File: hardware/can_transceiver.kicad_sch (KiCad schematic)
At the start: 4 parts, among them J3 CAN, U5 MCP2558FD-xSN

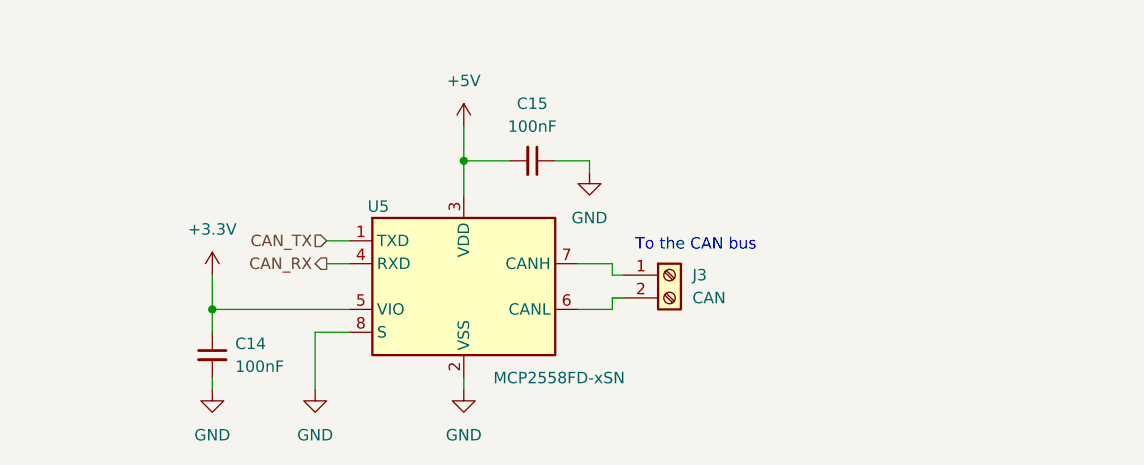
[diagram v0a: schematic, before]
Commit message: Improve the CAN transceiver circuit
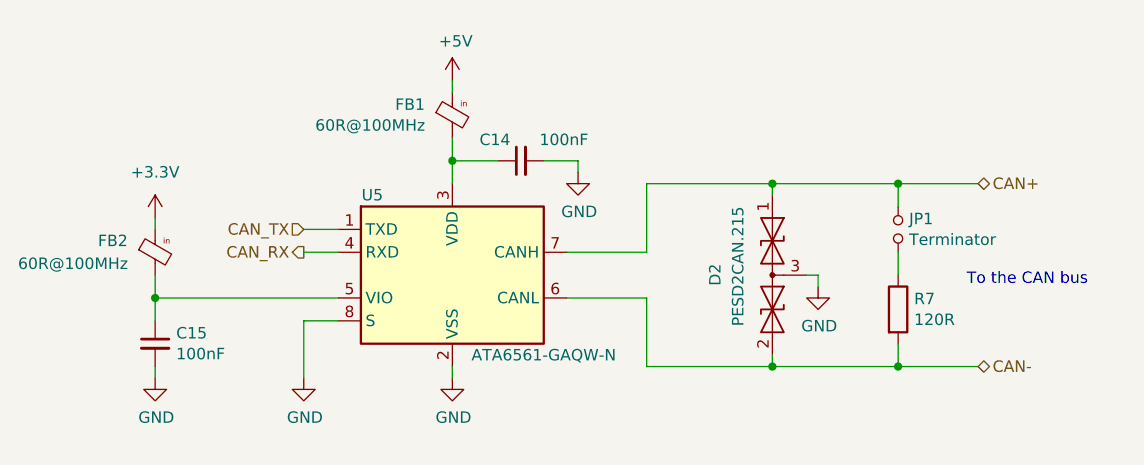
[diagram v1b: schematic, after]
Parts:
- removed J3: CAN, symbol Connector:Screw_Terminal_01x02
- added D2: PESD2CAN.215, Package_TO_SOT_SMD:SOT-23, symbol Local_Library:D_TVS_x2_AAC-Device
- added FB1, FB2: 60R@100MHz, Inductor_SMD:L_0603_1608Metric, symbol Local_Library:Ferrite_Bead_Small_PWR-PUTM_KICAD_SYMBOLS
- added JP1: Terminator, Connector_PinHeader_2.54mm:PinHeader_1x02_P2.54mm_Vertical, symbol Local_Library:Jumper_NO_Small-Device
- added R7: 120R, Resistor_SMD:R_0603_1608Metric, symbol Device:R
- C14, C15: footprint (none) -> Capacitor_SMD:C_0603_1608Metric
- U5: value MCP2558FD-xSN -> ATA6561-GAQW-N
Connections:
- net +3.3V: now also FB2.1; no longer C14.1, U5.5 (VIO)
- net +5V: now also FB1.1; no longer C15.2, U5.3 (VDD)
- net GND: now also C15.2, D2.3 (common); no longer C15.1
- net CAN-: now reaches U5.6 (CANL)
- net CAN-: now also D2.2 (A2), R7.2
- net CAN+: now reaches U5.7 (CANH)
- net CAN+: now also D2.1 (A1), JP1.1
- new net: C15.1, FB2.2, U5.5 (VIO)
- new net: JP1.2, R7.1
- new net: C14.1, FB1.2, U5.3 (VDD)
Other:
- company: PUT MotorSport -> PUT Motorsport

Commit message: Refactor the main sheet
- Replace screw connectors with a goldpin header
- Add reset button
- Add SWD debugger header
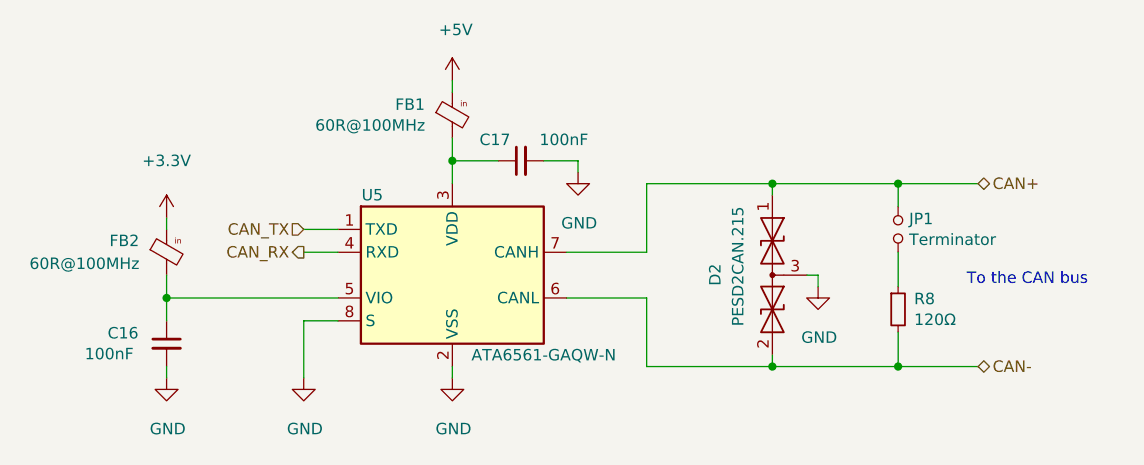
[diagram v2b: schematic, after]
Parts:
- R8: renamed from R7; value 120R -> 120Ω; symbol Device:R -> Device:R_Small
- renumbered C15 to C16, C14 to C17
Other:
- moved on the sheet: C16, FB2
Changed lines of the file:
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@@
   (junction (at 180.34 87.63) (diameter 0) (color 0 0 0 0)
   )
-  (junction (at 111.76 100.33) (diameter 0) (color 0 0 0 0)
+  (junction (at 113.03 100.33) (diameter 0) (color 0 0 0 0)
   )
   (wire (pts (xy 166.37 87.63) (xy 180.34 87.63))
@@
     (stroke (width 0) (type default) (color 0 0 0 0))
   )
-  (wire (pts (xy 194.31 105.41) (xy 194.31 107.95))
+  (wire (pts (xy 194.31 104.14) (xy 194.31 107.95))
     (stroke (width 0) (type default) (color 0 0 0 0))
   )
@@
     (stroke (width 0) (type default) (color 0 0 0 0))
   )
-  (wire (pts (xy 111.76 100.33) (xy 111.76 97.79))
+  (wire (pts (xy 194.31 95.25) (xy 194.31 99.06))
+    (stroke (width 0) (type default) (color 0 0 0 0))
+  )
+  (wire (pts (xy 113.03 100.33) (xy 113.03 97.79))
     (stroke (width 0) (type default) (color 0 0 0 0))
   )
@@
     (stroke (width 0) (type default) (color 0 0 0 0))
   )
-  (wire (pts (xy 111.76 100.33) (xy 111.76 102.87))
+  (wire (pts (xy 113.03 100.33) (xy 113.03 102.87))
     (stroke (width 0) (type default) (color 0 0 0 0))
   )
@@
     (stroke (width 0) (type default) (color 0 0 0 0))
   )
-  (wire (pts (xy 111.76 100.33) (xy 132.08 100.33))
+  (wire (pts (xy 113.03 100.33) (xy 132.08 100.33))
     (stroke (width 0) (type default) (color 0 0 0 0))
   )
@@
     (stroke (width 0) (type default) (color 0 0 0 0))
   )
-  (wire (pts (xy 111.76 91.44) (xy 111.76 92.71))
+  (wire (pts (xy 113.03 91.44) (xy 113.03 92.71))
     (stroke (width 0) (type default) (color 0 0 0 0))
   )
@@
     (stroke (width 0) (type default) (color 0 0 0 0))
   )
-  (wire (pts (xy 194.31 95.25) (xy 194.31 97.79))
-    (stroke (width 0) (type default) (color 0 0 0 0))
-  )
-  (wire (pts (xy 111.76 109.22) (xy 111.76 107.95))
+  (wire (pts (xy 113.03 109.22) (xy 113.03 107.95))
     (stroke (width 0) (type default) (color 0 0 0 0))
   )
@@
     (effects (font (size 1.27 1.27)) (justify right))
   )
-  (symbol (lib_id "Local_Library:Ferrite_Bead_Small_PWR-PUTM_KICAD_SYMBOLS") (at 111.76 95.25 0) (unit 1)
-    (in_bom yes) (on_board yes)
-    (property "Reference" "FB2" (id 0) (at 105.41 93.98 0)
-      (effects (font (size 1.27 1.27)) (justify left))
-    )
-    (property "Value" "60R@100MHz" (id 1) (at 96.52 96.52 0)
-      (effects (font (size 1.27 1.27)) (justify left))
-    )
-    (property "Footprint" "Inductor_SMD:L_0603_1608Metric" (id 2) (at 109.982 95.25 90)
-      (effects (font (size 1.27 1.27)) hide)
-    )
-    (property "Datasheet" "~" (id 3) (at 111.76 95.25 0)
+  (symbol (lib_id "Local_Library:Ferrite_Bead_Small_PWR-PUTM_KICAD_SYMBOLS") (at 113.03 95.25 0) (unit 1)
+    (in_bom yes) (on_board yes)
+    (property "Reference" "FB2" (id 0) (at 106.68 93.98 0)
+      (effects (font (size 1.27 1.27)) (justify left))
+    )
+    (property "Value" "60R@100MHz" (id 1) (at 97.79 96.52 0)
+      (effects (font (size 1.27 1.27)) (justify left))
+    )
+    (property "Footprint" "Inductor_SMD:L_0603_1608Metric" (id 2) (at 111.252 95.25 90)
+      (effects (font (size 1.27 1.27)) hide)
+    )
+    (property "Datasheet" "~" (id 3) (at 113.03 95.25 0)
       (effects (font (size 1.27 1.27)) hide)
     )
@@
       (effects (font (size 1.27 1.27)) hide)
     )
-    (property "Value" "GND" (id 1) (at 128.397 113.6142 0))
+    (property "Value" "GND" (id 1) (at 128.397 114.8842 0))
     (property "Footprint" "" (id 2) (at 128.27 109.22 0)
       (effects (font (size 1.27 1.27)) hide)
@@
       (effects (font (size 1.27 1.27)) hide)
     )
-    (property "Value" "GND" (id 1) (at 185.547 103.4542 0))
+    (property "Value" "GND" (id 1) (at 185.547 104.7242 0))
     (property "Footprint" "" (id 2) (at 185.42 99.06 0)
       (effects (font (size 1.27 1.27)) hide)
@@
       (effects (font (size 1.27 1.27)) hide)
     )
-    (property "Value" "GND" (id 1) (at 144.907 113.6142 0))
+    (property "Value" "GND" (id 1) (at 144.907 114.8842 0))
     (property "Footprint" "" (id 2) (at 144.78 109.22 0)
       (effects (font (size 1.27 1.27)) hide)
@@
     (pin "1")
   )
-  (symbol (lib_id "Device:C_Small") (at 111.76 105.41 0) (unit 1)
-    (in_bom yes) (on_board yes)
-    (property "Reference" "C15" (id 0) (at 114.0968 104.2416 0)
-      (effects (font (size 1.27 1.27)) (justify left))
-    )
-    (property "Value" "100nF" (id 1) (at 114.0968 106.553 0)
-      (effects (font (size 1.27 1.27)) (justify left))
-    )
-    (property "Footprint" "Capacitor_SMD:C_0603_1608Metric" (id 2) (at 111.76 105.41 0)
-      (effects (font (size 1.27 1.27)) hide)
-    )
-    (property "Datasheet" "~" (id 3) (at 111.76 105.41 0)
+  (symbol (lib_id "Device:C_Small") (at 113.03 105.41 0) (unit 1)
+    (in_bom yes) (on_board yes)
+    (property "Reference" "C16" (id 0) (at 106.4768 104.2416 0)
+      (effects (font (size 1.27 1.27)) (justify left))
+    )
+    (property "Value" "100nF" (id 1) (at 103.9368 106.553 0)
+      (effects (font (size 1.27 1.27)) (justify left))
+    )
+    (property "Footprint" "Capacitor_SMD:C_0603_1608Metric" (id 2) (at 113.03 105.41 0)
+      (effects (font (size 1.27 1.27)) hide)
+    )
+    (property "Datasheet" "~" (id 3) (at 113.03 105.41 0)
       (effects (font (size 1.27 1.27)) hide)
     )
@@
   (symbol (lib_id "Device:C_Small") (at 152.4 85.09 90) (unit 1)
     (in_bom yes) (on_board yes)
-    (property "Reference" "C14" (id 0) (at 151.2316 82.7532 90)
+    (property "Reference" "C17" (id 0) (at 151.2316 82.7532 90)
       (effects (font (size 1.27 1.27)) (justify left))
     )
@@
     (pin "2")
   )
-  (symbol (lib_id "power:GND") (at 111.76 109.22 0) (unit 1)
-    (in_bom yes) (on_board yes)
-    (property "Reference" "#U0103" (id 0) (at 111.76 115.57 0)
-      (effects (font (size 1.27 1.27)) hide)
-    )
-    (property "Value" "GND" (id 1) (at 111.887 113.6142 0))
-    (property "Footprint" "" (id 2) (at 111.76 109.22 0)
-      (effects (font (size 1.27 1.27)) hide)
-    )
-    (property "Datasheet" "" (id 3) (at 111.76 109.22 0)
+  (symbol (lib_id "power:GND") (at 113.03 109.22 0) (unit 1)
+    (in_bom yes) (on_board yes)
+    (property "Reference" "#U0103" (id 0) (at 113.03 115.57 0)
+      (effects (font (size 1.27 1.27)) hide)
+    )
+    (property "Value" "GND" (id 1) (at 113.157 114.8842 0))
+    (property "Footprint" "" (id 2) (at 113.03 109.22 0)
+      (effects (font (size 1.27 1.27)) hide)
+    )
+    (property "Datasheet" "" (id 3) (at 113.03 109.22 0)
       (effects (font (size 1.27 1.27)) hide)
     )
@@
       (effects (font (size 1.27 1.27)) hide)
     )
-    (property "Value" "GND" (id 1) (at 158.877 90.7542 0))
+    (property "Value" "GND" (id 1) (at 158.877 92.0242 0))
     (property "Footprint" "" (id 2) (at 158.75 86.36 0)
       (effects (font (size 1.27 1.27)) hide)
@@
     (pin "1")
   )
-  (symbol (lib_id "power:+3.3V") (at 111.76 91.44 0) (unit 1)
-    (in_bom yes) (on_board yes) (fields_autoplaced)
-    (property "Reference" "#PWR0102" (id 0) (at 111.76 95.25 0)
-      (effects (font (size 1.27 1.27)) hide)
-    )
-    (property "Value" "+3.3V" (id 1) (at 111.76 86.36 0))
-    (property "Footprint" "" (id 2) (at 111.76 91.44 0)
-      (effects (font (size 1.27 1.27)) hide)
-    )
-    (property "Datasheet" "" (id 3) (at 111.76 91.44 0)
-      (effects (font (size 1.27 1.27)) hide)
-    )
-    (pin "1")
-  )
-  (symbol (lib_id "Device:R") (at 194.31 101.6 0) (unit 1)
-    (in_bom yes) (on_board yes)
-    (property "Reference" "R7" (id 0) (at 196.088 100.4316 0)
-      (effects (font (size 1.27 1.27)) (justify left))
-    )
-    (property "Value" "120R" (id 1) (at 196.088 102.743 0)
-      (effects (font (size 1.27 1.27)) (justify left))
-    )
-    (property "Footprint" "Resistor_SMD:R_0603_1608Metric" (id 2) (at 192.532 101.6 90)
+  (symbol (lib_id "power:+3.3V") (at 113.03 91.44 0) (unit 1)
+    (in_bom yes) (on_board yes)
+    (property "Reference" "#PWR0102" (id 0) (at 113.03 95.25 0)
+      (effects (font (size 1.27 1.27)) hide)
+    )
+    (property "Value" "+3.3V" (id 1) (at 113.03 85.09 0))
+    (property "Footprint" "" (id 2) (at 113.03 91.44 0)
+      (effects (font (size 1.27 1.27)) hide)
+    )
+    (property "Datasheet" "" (id 3) (at 113.03 91.44 0)
+      (effects (font (size 1.27 1.27)) hide)
+    )
+    (pin "1")
+  )
+  (symbol (lib_id "Device:R_Small") (at 194.31 101.6 0) (unit 1)
+    (in_bom yes) (on_board yes)
+    (property "Reference" "R8" (id 0) (at 196.088 100.4316 0)
+      (effects (font (size 1.27 1.27)) (justify left))
+    )
+    (property "Value" "120Ω" (id 1) (at 196.088 102.743 0)
+      (effects (font (size 1.27 1.27)) (justify left))
+    )
+    (property "Footprint" "Resistor_SMD:R_0603_1608Metric" (id 2) (at 194.31 101.6 0)
       (effects (font (size 1.27 1.27)) hide)
     )
@@
       (effects (font (size 1.27 1.27)) hide)
     )
-    (property "Value" "+5V" (id 1) (at 145.161 71.8058 0))
+    (property "Value" "+5V" (id 1) (at 145.161 70.5358 0))
     (property "Footprint" "" (id 2) (at 144.78 76.2 0)
       (effects (font (size 1.27 1.27)) hide)

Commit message: Add ADC circuit
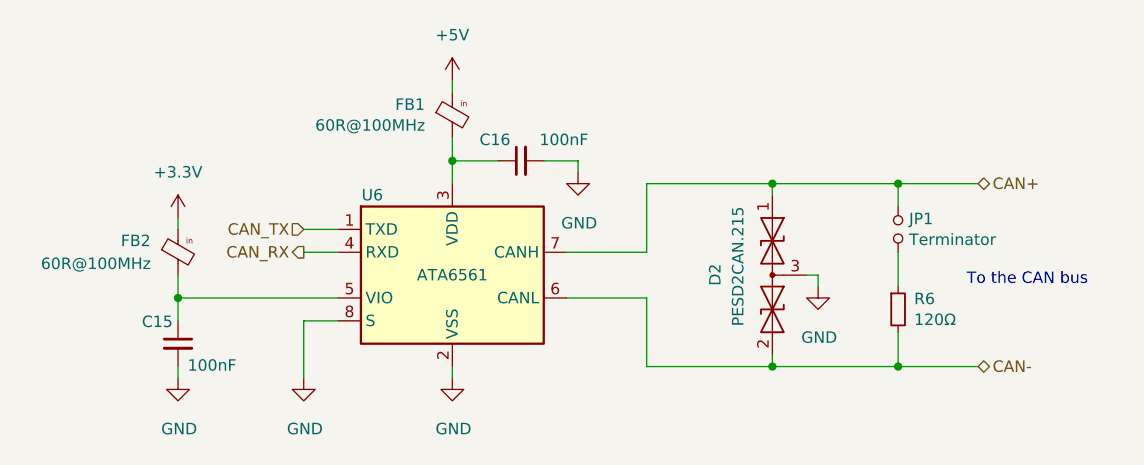
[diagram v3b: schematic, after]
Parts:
- U6: renamed from U5; value ATA6561-GAQW-N -> ATA6561
- renumbered C16 to C15, C17 to C16, R8 to R6
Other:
- moved on the sheet: C15, FB2
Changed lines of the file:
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@@
   (title_block
     (title "CAN Transceiver")
-    (date "2022-11-21")
+    (date "2022-12-04")
     (rev "0.1.0")
     (company "PUT Motorsport")
+    (comment 1 "Author: I. Kajdan")
   )
   (junction (at 180.34 107.95) (diameter 0) (color 0 0 0 0)
@@
   (junction (at 180.34 87.63) (diameter 0) (color 0 0 0 0)
   )
-  (junction (at 113.03 100.33) (diameter 0) (color 0 0 0 0)
+  (junction (at 114.3 100.33) (diameter 0) (color 0 0 0 0)
   )
   (wire (pts (xy 166.37 87.63) (xy 180.34 87.63))
@@
     (stroke (width 0) (type default) (color 0 0 0 0))
   )
-  (wire (pts (xy 113.03 100.33) (xy 113.03 97.79))
+  (wire (pts (xy 114.3 100.33) (xy 114.3 97.79))
     (stroke (width 0) (type default) (color 0 0 0 0))
   )
@@
     (stroke (width 0) (type default) (color 0 0 0 0))
   )
-  (wire (pts (xy 113.03 100.33) (xy 113.03 102.87))
+  (wire (pts (xy 114.3 100.33) (xy 114.3 102.87))
     (stroke (width 0) (type default) (color 0 0 0 0))
   )
@@
     (stroke (width 0) (type default) (color 0 0 0 0))
   )
-  (wire (pts (xy 113.03 100.33) (xy 132.08 100.33))
+  (wire (pts (xy 114.3 100.33) (xy 132.08 100.33))
     (stroke (width 0) (type default) (color 0 0 0 0))
   )
@@
     (stroke (width 0) (type default) (color 0 0 0 0))
   )
-  (wire (pts (xy 113.03 91.44) (xy 113.03 92.71))
+  (wire (pts (xy 114.3 91.44) (xy 114.3 92.71))
     (stroke (width 0) (type default) (color 0 0 0 0))
   )
@@
     (stroke (width 0) (type default) (color 0 0 0 0))
   )
-  (wire (pts (xy 113.03 109.22) (xy 113.03 107.95))
+  (wire (pts (xy 114.3 109.22) (xy 114.3 107.95))
     (stroke (width 0) (type default) (color 0 0 0 0))
   )
@@
     (effects (font (size 1.27 1.27)) (justify right))
   )
-  (symbol (lib_id "Local_Library:Ferrite_Bead_Small_PWR-PUTM_KICAD_SYMBOLS") (at 113.03 95.25 0) (unit 1)
-    (in_bom yes) (on_board yes)
-    (property "Reference" "FB2" (id 0) (at 106.68 93.98 0)
-      (effects (font (size 1.27 1.27)) (justify left))
-    )
-    (property "Value" "60R@100MHz" (id 1) (at 97.79 96.52 0)
-      (effects (font (size 1.27 1.27)) (justify left))
-    )
-    (property "Footprint" "Inductor_SMD:L_0603_1608Metric" (id 2) (at 111.252 95.25 90)
-      (effects (font (size 1.27 1.27)) hide)
-    )
-    (property "Datasheet" "~" (id 3) (at 113.03 95.25 0)
+  (symbol (lib_id "Local_Library:Ferrite_Bead_Small_PWR-PUTM_KICAD_SYMBOLS") (at 114.3 95.25 0) (unit 1)
+    (in_bom yes) (on_board yes)
+    (property "Reference" "FB2" (id 0) (at 107.95 93.98 0)
+      (effects (font (size 1.27 1.27)) (justify left))
+    )
+    (property "Value" "60R@100MHz" (id 1) (at 99.06 96.52 0)
+      (effects (font (size 1.27 1.27)) (justify left))
+    )
+    (property "Footprint" "Inductor_SMD:L_0603_1608Metric" (id 2) (at 112.522 95.25 90)
+      (effects (font (size 1.27 1.27)) hide)
+    )
+    (property "Datasheet" "~" (id 3) (at 114.3 95.25 0)
       (effects (font (size 1.27 1.27)) hide)
     )
@@
     (pin "1")
   )
-  (symbol (lib_id "Device:C_Small") (at 113.03 105.41 0) (unit 1)
-    (in_bom yes) (on_board yes)
-    (property "Reference" "C16" (id 0) (at 106.4768 104.2416 0)
-      (effects (font (size 1.27 1.27)) (justify left))
-    )
-    (property "Value" "100nF" (id 1) (at 103.9368 106.553 0)
-      (effects (font (size 1.27 1.27)) (justify left))
-    )
-    (property "Footprint" "Capacitor_SMD:C_0603_1608Metric" (id 2) (at 113.03 105.41 0)
-      (effects (font (size 1.27 1.27)) hide)
-    )
-    (property "Datasheet" "~" (id 3) (at 113.03 105.41 0)
+  (symbol (lib_id "Device:C_Small") (at 114.3 105.41 0) (unit 1)
+    (in_bom yes) (on_board yes)
+    (property "Reference" "C15" (id 0) (at 110.2868 102.9716 0)
+      (effects (font (size 1.27 1.27)) (justify left))
+    )
+    (property "Value" "100nF" (id 1) (at 115.3668 107.823 0)
+      (effects (font (size 1.27 1.27)) (justify left))
+    )
+    (property "Footprint" "Capacitor_SMD:C_0603_1608Metric" (id 2) (at 114.3 105.41 0)
+      (effects (font (size 1.27 1.27)) hide)
+    )
+    (property "Datasheet" "~" (id 3) (at 114.3 105.41 0)
       (effects (font (size 1.27 1.27)) hide)
     )
@@
   (symbol (lib_id "Device:C_Small") (at 152.4 85.09 90) (unit 1)
     (in_bom yes) (on_board yes)
-    (property "Reference" "C17" (id 0) (at 151.2316 82.7532 90)
+    (property "Reference" "C16" (id 0) (at 151.2316 82.7532 90)
       (effects (font (size 1.27 1.27)) (justify left))
     )
@@
     (pin "2")
   )
-  (symbol (lib_id "power:GND") (at 113.03 109.22 0) (unit 1)
-    (in_bom yes) (on_board yes)
-    (property "Reference" "#U0103" (id 0) (at 113.03 115.57 0)
-      (effects (font (size 1.27 1.27)) hide)
-    )
-    (property "Value" "GND" (id 1) (at 113.157 114.8842 0))
-    (property "Footprint" "" (id 2) (at 113.03 109.22 0)
-      (effects (font (size 1.27 1.27)) hide)
-    )
-    (property "Datasheet" "" (id 3) (at 113.03 109.22 0)
+  (symbol (lib_id "power:GND") (at 114.3 109.22 0) (unit 1)
+    (in_bom yes) (on_board yes)
+    (property "Reference" "#U0103" (id 0) (at 114.3 115.57 0)
+      (effects (font (size 1.27 1.27)) hide)
+    )
+    (property "Value" "GND" (id 1) (at 114.427 114.8842 0))
+    (property "Footprint" "" (id 2) (at 114.3 109.22 0)
+      (effects (font (size 1.27 1.27)) hide)
+    )
+    (property "Datasheet" "" (id 3) (at 114.3 109.22 0)
+      (effects (font (size 1.27 1.27)) hide)
+    )
+    (pin "1")
+  )
+  (symbol (lib_id "power:+5V") (at 144.78 76.2 0) (unit 1)
+    (in_bom yes) (on_board yes)
+    (property "Reference" "#PWR019" (id 0) (at 144.78 80.01 0)
+      (effects (font (size 1.27 1.27)) hide)
+    )
+    (property "Value" "+5V" (id 1) (at 144.78 71.12 0))
+    (property "Footprint" "" (id 2) (at 144.78 76.2 0)
+      (effects (font (size 1.27 1.27)) hide)
+    )
+    (property "Datasheet" "" (id 3) (at 144.78 76.2 0)
       (effects (font (size 1.27 1.27)) hide)
     )
@@
     (pin "1")
   )
-  (symbol (lib_id "power:+3.3V") (at 113.03 91.44 0) (unit 1)
-    (in_bom yes) (on_board yes)
-    (property "Reference" "#PWR0102" (id 0) (at 113.03 95.25 0)
-      (effects (font (size 1.27 1.27)) hide)
-    )
-    (property "Value" "+3.3V" (id 1) (at 113.03 85.09 0))
-    (property "Footprint" "" (id 2) (at 113.03 91.44 0)
-      (effects (font (size 1.27 1.27)) hide)
-    )
-    (property "Datasheet" "" (id 3) (at 113.03 91.44 0)
+  (symbol (lib_id "power:+3.3V") (at 114.3 91.44 0) (unit 1)
+    (in_bom yes) (on_board yes)
+    (property "Reference" "#PWR0102" (id 0) (at 114.3 95.25 0)
+      (effects (font (size 1.27 1.27)) hide)
+    )
+    (property "Value" "+3.3V" (id 1) (at 114.3 86.36 0))
+    (property "Footprint" "" (id 2) (at 114.3 91.44 0)
+      (effects (font (size 1.27 1.27)) hide)
+    )
+    (property "Datasheet" "" (id 3) (at 114.3 91.44 0)
       (effects (font (size 1.27 1.27)) hide)
     )
@@
   (symbol (lib_id "Device:R_Small") (at 194.31 101.6 0) (unit 1)
     (in_bom yes) (on_board yes)
-    (property "Reference" "R8" (id 0) (at 196.088 100.4316 0)
+    (property "Reference" "R6" (id 0) (at 196.088 100.4316 0)
       (effects (font (size 1.27 1.27)) (justify left))
     )
@@
     (pin "2")
   )
-  (symbol (lib_id "power:+5V") (at 144.78 76.2 0) (unit 1)
-    (in_bom yes) (on_board yes)
-    (property "Reference" "#U0101" (id 0) (at 144.78 80.01 0)
-      (effects (font (size 1.27 1.27)) hide)
-    )
-    (property "Value" "+5V" (id 1) (at 145.161 70.5358 0))
-    (property "Footprint" "" (id 2) (at 144.78 76.2 0)
-      (effects (font (size 1.27 1.27)) hide)
-    )
-    (property "Datasheet" "" (id 3) (at 144.78 76.2 0)
-      (effects (font (size 1.27 1.27)) hide)
-    )
-    (pin "1")
-  )
   (symbol (lib_id "Interface_CAN_LIN:MCP2558FD-xSN") (at 144.78 97.79 0) (unit 1)
     (in_bom yes) (on_board yes)
-    (property "Reference" "U5" (id 0) (at 135.89 88.9 0))
-    (property "Value" "ATA6561-GAQW-N" (id 1) (at 154.94 106.68 0))
+    (property "Reference" "U6" (id 0) (at 135.89 88.9 0))
+    (property "Value" "ATA6561" (id 1) (at 144.78 97.79 0))
     (property "Footprint" "Package_SO:SOIC-8_3.9x4.9mm_P1.27mm" (id 2) (at 144.78 113.03 0)
       (effects (font (size 1.27 1.27)) hide)
